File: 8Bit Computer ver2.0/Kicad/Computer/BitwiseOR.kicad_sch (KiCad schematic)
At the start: 5 parts, among them IC34 SN74LVC1G14DBVR, IC35 SN74HCS86DR, IC38 SN74HCS86DR, IC39 SN74HCS74DR, IC40 SN74HCS574DGSR

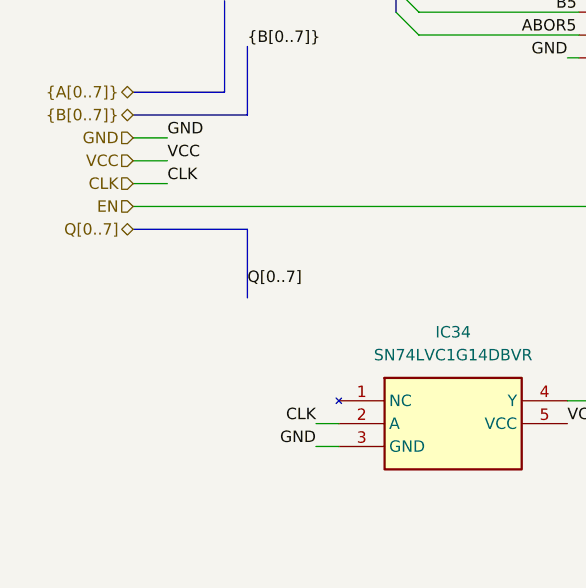
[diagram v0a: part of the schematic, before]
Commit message: Kicad,parts
Kicad:
added FlagRegister
began Inc, Comp
parts:
added comparator for P>Q 682
added faster sram 12ns AS7C
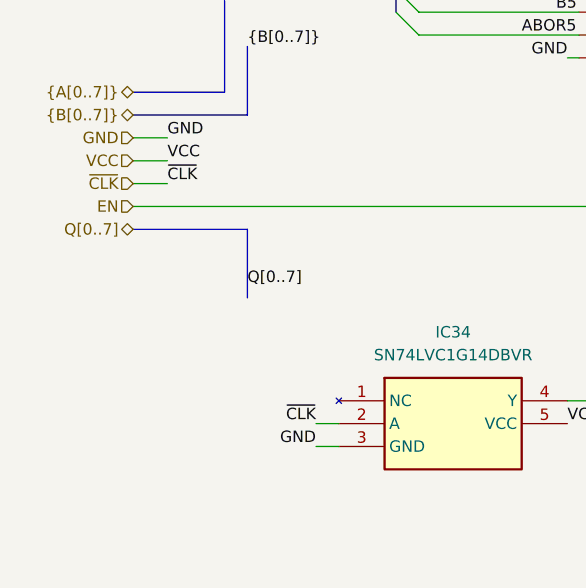
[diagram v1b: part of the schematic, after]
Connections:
- net CLK renamed ~{CLK}
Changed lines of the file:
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@@
 		)
 	)
-	(label "CLK"
+	(label "~{CLK}"
 		(at 48.26 101.6 0)
 		(effects
@@
 		)
 	)
-	(label "CLK"
+	(label "~{CLK}"
 		(at 64.77 128.27 180)
 		(effects
@@
 		)
 	)
-	(hierarchical_label "CLK"
+	(hierarchical_label "~{CLK}"
 		(shape input)
 		(at 44.45 101.6 180)

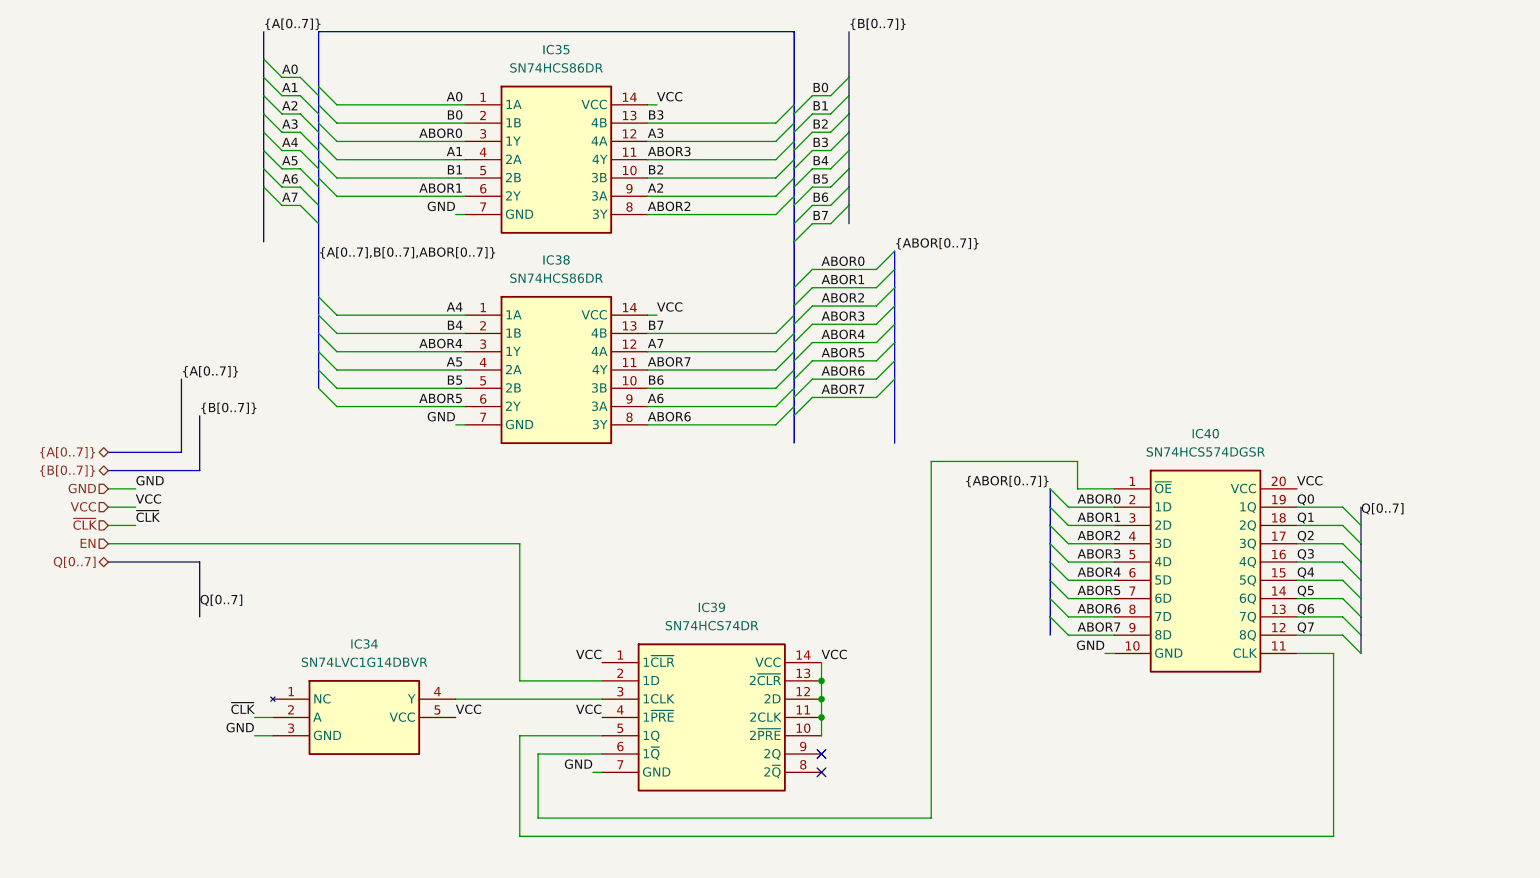
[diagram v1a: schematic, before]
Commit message: parts,Kicad
parts:
changed 8xDlatch HCS to ABT 574
waiting for SRAM CAD Model
Kicad:
imported AHC types of ICs
added ProgrammeCounter
finished Comparator
changed all HCS to AHC except 3in OR ->no AHC Version
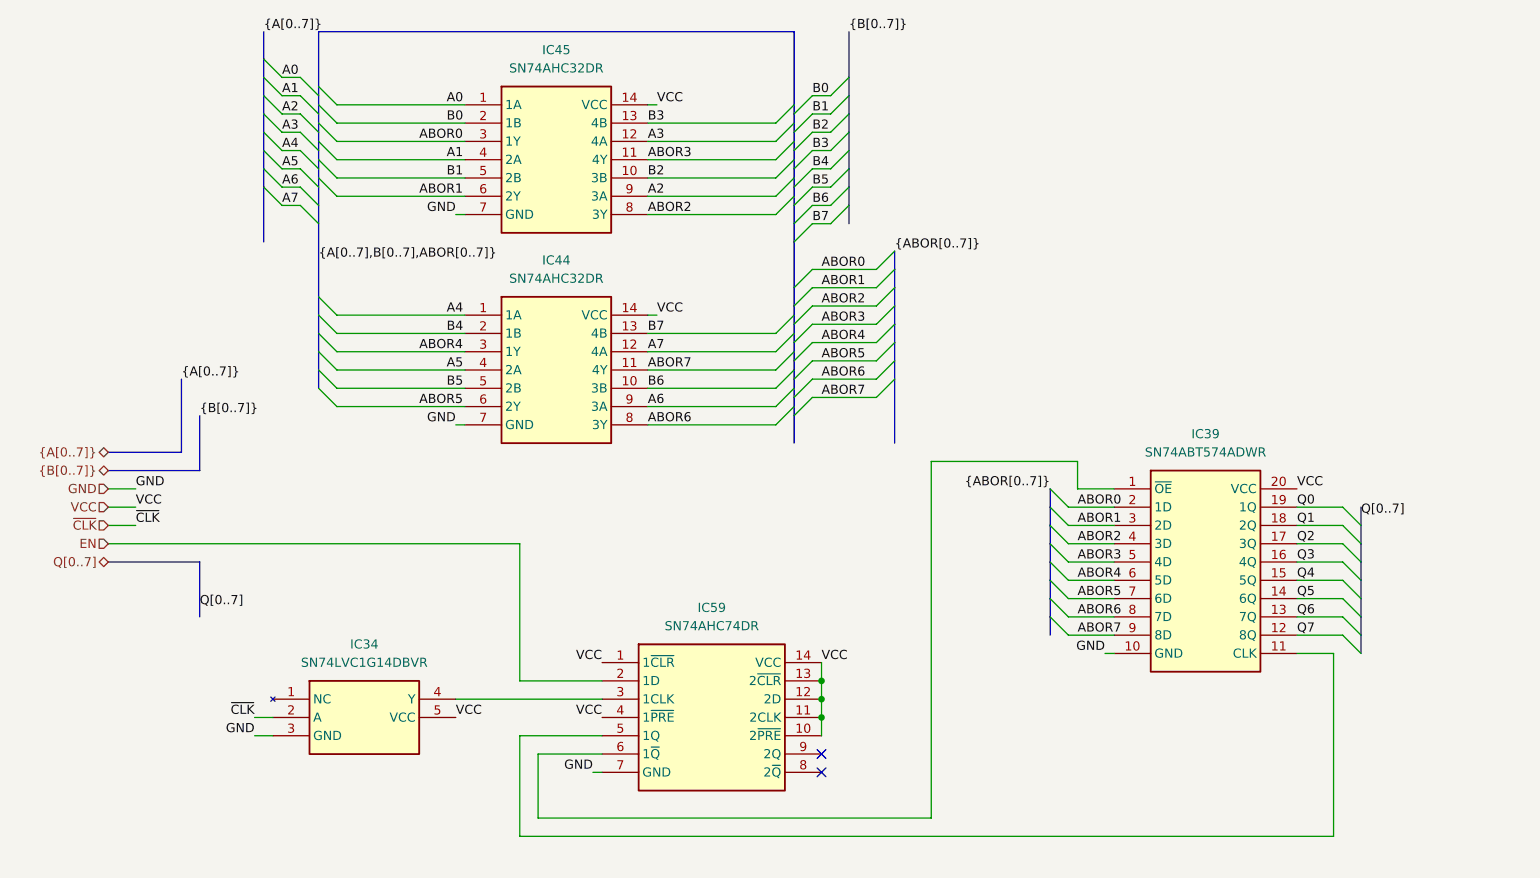
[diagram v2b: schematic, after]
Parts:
- removed IC35, IC38: SN74HCS86DR, Samacsys:SOIC127P600X175-14N, symbol Samacsys:SN74HCS86DR
- removed IC39: SN74HCS74DR, Samacsys:SOIC127P600X175-14N, symbol Samacsys:SN74HCS74DR
- removed IC40: SN74HCS574DGSR, Samacsys:SOP50P490X110-20N, symbol Samacsys:SN74HCS574DGSR
- added IC39: SN74ABT574ADWR, Samacsys:SOIC127P1030X265-20N, symbol Samacsys:SN74ABT574ADWR
- added IC44, IC45: SN74AHC32DR, Samacsys:SOIC127P600X175-14N, symbol Samacsys:SN74AHC32DR
- added IC59: SN74AHC74DR, Samacsys:SOIC127P600X175-14N, symbol Samacsys:SN74AHC74DR
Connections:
- net A0: now also IC45.1 (1A)
- net A1: now also IC45.4 (2A)
- net A2: now also IC45.9 (3A)
- net A3: now also IC45.12 (4A)
- net A4: now also IC44.1 (1A)
- net A5: now also IC44.4 (2A)
- net A6: now also IC44.9 (3A)
- net A7: now also IC44.12 (4A)
- net ABOR0: now also IC39.2 (1D), IC45.3 (1Y)
- net ABOR1: now also IC39.3 (2D), IC45.6 (2Y)
- net ABOR2: now also IC39.4 (3D), IC45.8 (3Y)
- net ABOR3: now also IC39.5 (4D), IC45.11 (4Y)
- net ABOR4: now also IC39.6 (5D), IC44.3 (1Y)
- net ABOR5: now also IC39.7 (6D), IC44.6 (2Y)
- net ABOR6: now also IC39.8 (7D), IC44.8 (3Y)
- net ABOR7: now also IC39.9 (8D), IC44.11 (4Y)
- net B0: now also IC45.2 (1B)
- net B1: now also IC45.5 (2B)
- net B2: now also IC45.10 (3B)
- net B3: now also IC45.13 (4B)
- net B4: now also IC44.2 (1B)
- net B5: now also IC44.5 (2B)
- net B6: now also IC44.10 (3B)
- net B7: now also IC44.13 (4B)
- net EN: now also IC59.2 (1D)
- net GND: now also IC39.10 (GND), IC44.7 (GND), IC45.7 (GND), IC59.7 (GND)
- net Q0: now also IC39.19 (1Q)
- net Q1: now also IC39.18 (2Q)
- net Q2: now also IC39.17 (3Q)
- net Q3: now also IC39.16 (4Q)
- net Q4: now also IC39.15 (5Q)
- net Q5: now also IC39.14 (6Q)
- net Q6: now also IC39.13 (7Q)
- net Q7: now also IC39.12 (8Q)
- net VCC: now also IC39.20 (VCC), IC44.14 (VCC), IC45.14 (VCC), IC59.1 (1~{CLR}), IC59.10 (2~{PRE}), IC59.11 (2CLK), IC59.12 (2D), IC59.13 (2~{CLR}), IC59.14 (VCC), IC59.4 (1~{PRE})
- net at IC34.4 (Y): now also IC59.3 (1CLK)
- new net: IC39.1 (~{OE}), IC59.6 (1~{Q})
- new net: IC39.11 (CLK), IC59.5 (1Q)

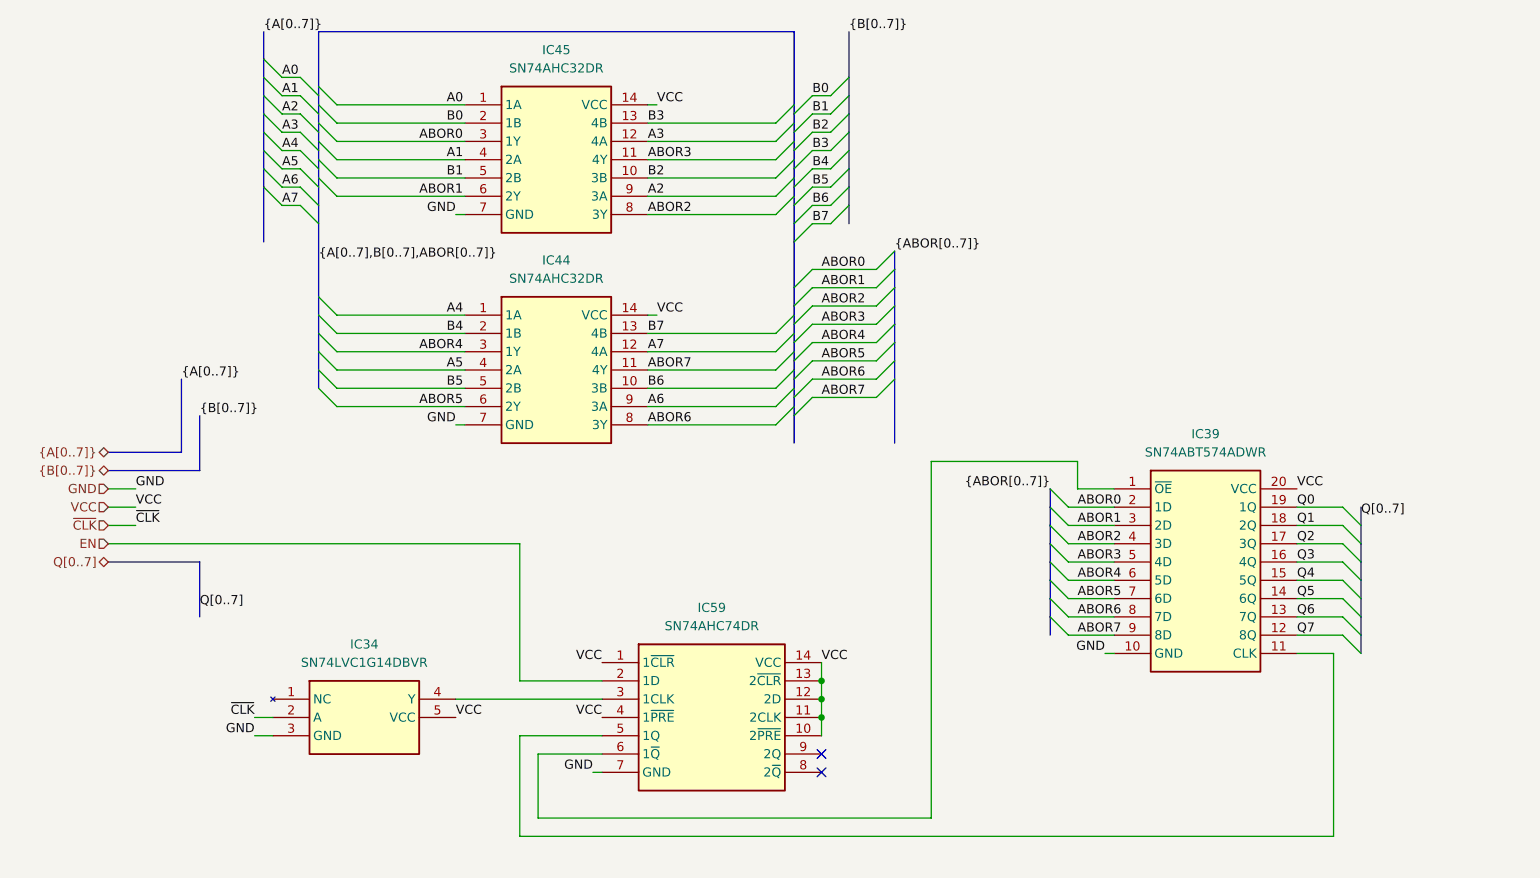
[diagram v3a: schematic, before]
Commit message: Kicad, parts
Parts:
added Leds
Kicad:
added Input Output
changed Q bus to DAT bus
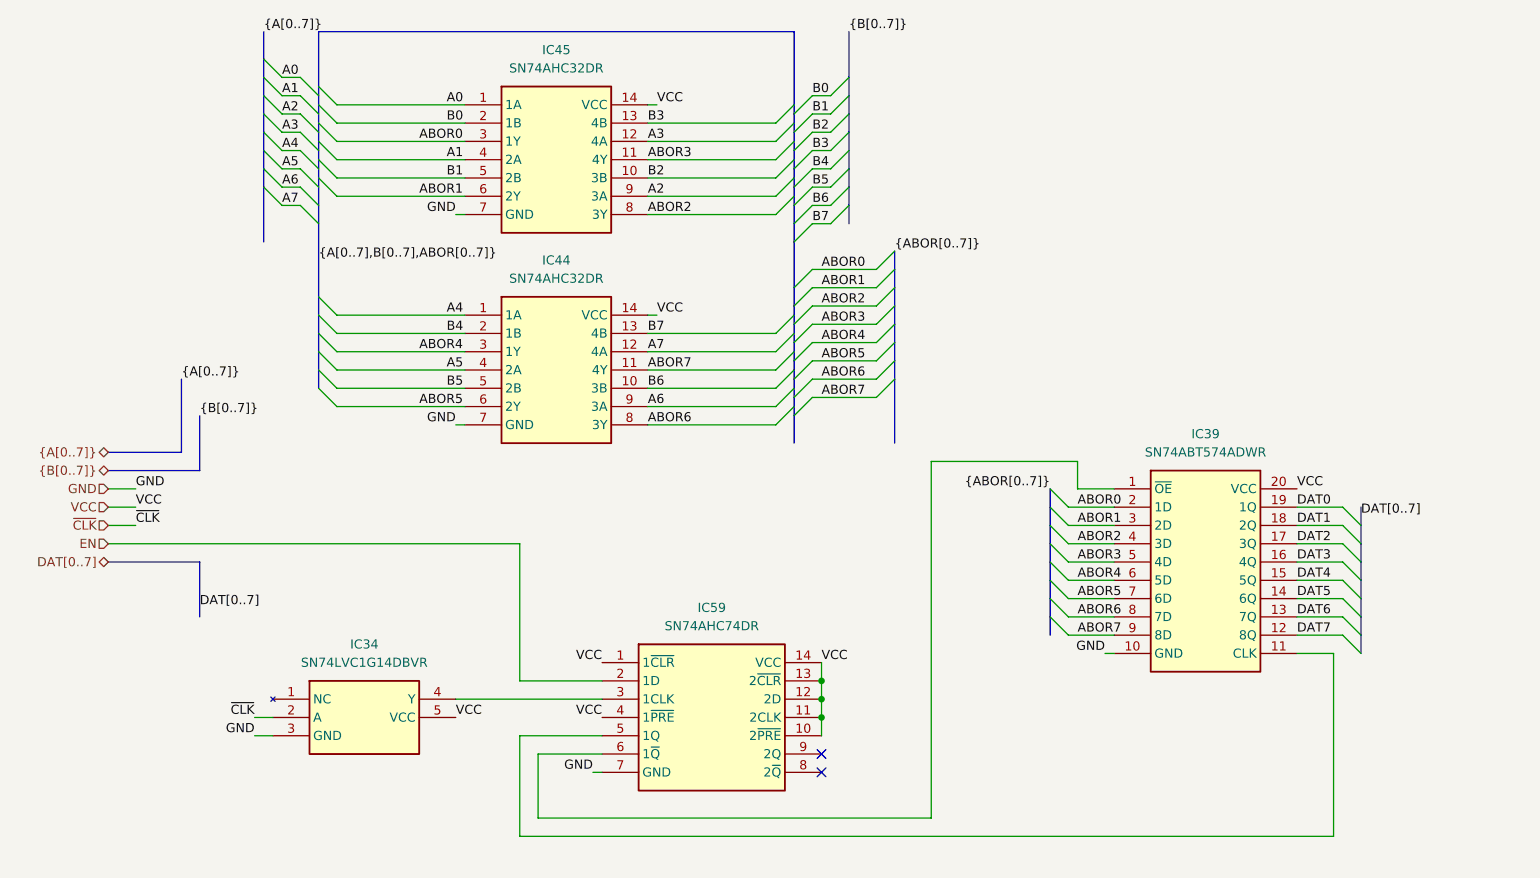
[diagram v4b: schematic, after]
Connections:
- net Q0 renamed DAT0
- net Q1 renamed DAT1
- net Q2 renamed DAT2
- net Q3 renamed DAT3
- net Q4 renamed DAT4
- net Q5 renamed DAT5
- net Q6 renamed DAT6
- net Q7 renamed DAT7
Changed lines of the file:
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@@
 		)
 	)
-	(label "Q7"
+	(label "DAT7"
 		(at 209.55 116.84 0)
 		(effects
@@
 		)
 	)
-	(label "Q5"
+	(label "DAT5"
 		(at 209.55 111.76 0)
 		(effects
@@
 		)
 	)
-	(label "Q3"
+	(label "DAT3"
 		(at 209.55 106.68 0)
 		(effects
@@
 		)
 	)
-	(label "Q6"
+	(label "DAT6"
 		(at 209.55 114.3 0)
 		(effects
@@
 		)
 	)
-	(label "Q[0..7]"
+	(label "DAT[0..7]"
 		(at 218.44 100.33 0)
 		(effects
@@
 		)
 	)
-	(label "Q4"
+	(label "DAT4"
 		(at 209.55 109.22 0)
 		(effects
@@
 		)
 	)
-	(label "Q1"
+	(label "DAT1"
 		(at 209.55 101.6 0)
 		(effects
@@
 		)
 	)
-	(label "Q2"
+	(label "DAT2"
 		(at 209.55 104.14 0)
 		(effects
@@
 		)
 	)
-	(label "Q[0..7]"
+	(label "DAT[0..7]"
 		(at 57.15 113.03 0)
 		(effects
@@
 		)
 	)
-	(label "Q0"
+	(label "DAT0"
 		(at 209.55 99.06 0)
 		(effects
@@
 		)
 	)
-	(hierarchical_label "Q[0..7]"
+	(hierarchical_label "DAT[0..7]"
 		(shape tri_state)
 		(at 44.45 106.68 180)

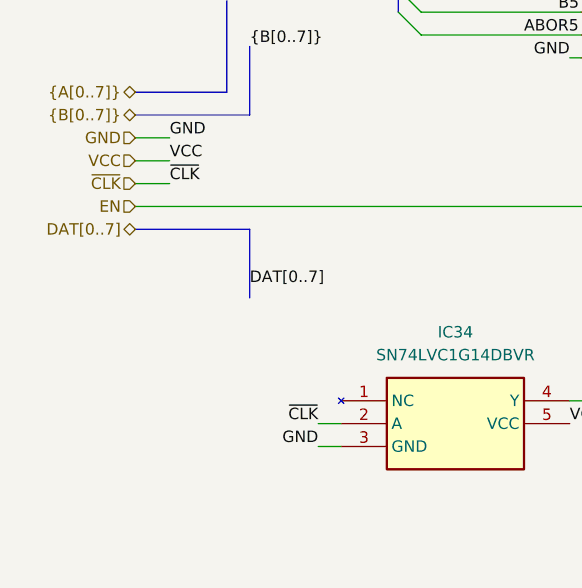
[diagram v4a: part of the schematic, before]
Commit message: Kicad, parts
parts:
added USB C PD Triggerboard
added Delay Chip for 90ns
added Push Button
Kicad:
added USB C PD Triggerboard
added rising edge detector via Delay and Xor for Accept Push Button
added VBUS net
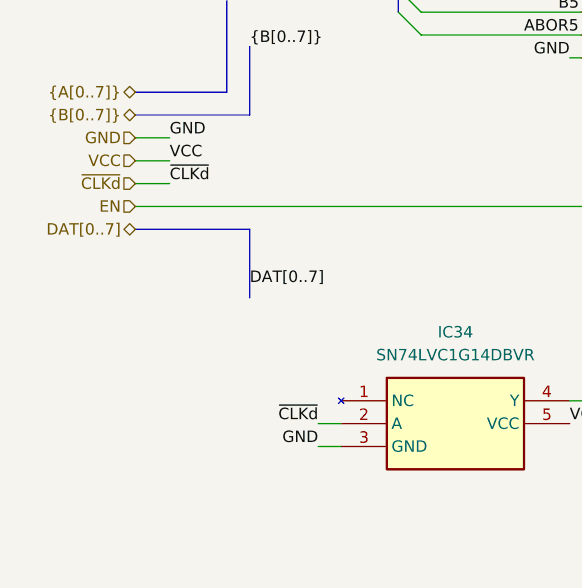
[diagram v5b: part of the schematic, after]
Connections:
- net ~{CLK} renamed ~{CLKd}
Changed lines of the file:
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@@
 		)
 	)
-	(label "~{CLK}"
+	(label "~{CLKd}"
 		(at 48.26 101.6 0)
 		(effects
@@
 		)
 	)
-	(label "~{CLK}"
+	(label "~{CLKd}"
 		(at 64.77 128.27 180)
 		(effects
@@
 		)
 	)
-	(hierarchical_label "~{CLK}"
+	(hierarchical_label "~{CLKd}"
 		(shape input)
 		(at 44.45 101.6 180)
